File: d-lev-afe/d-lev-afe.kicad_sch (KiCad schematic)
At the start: 26 parts, among them J1 S8B-PH-SM4-TB, Q1 MMBT3904, Q2 MMBT3906, U1 74AHC04, U2 HT7533-1-SOT89, U3 SRV05-4

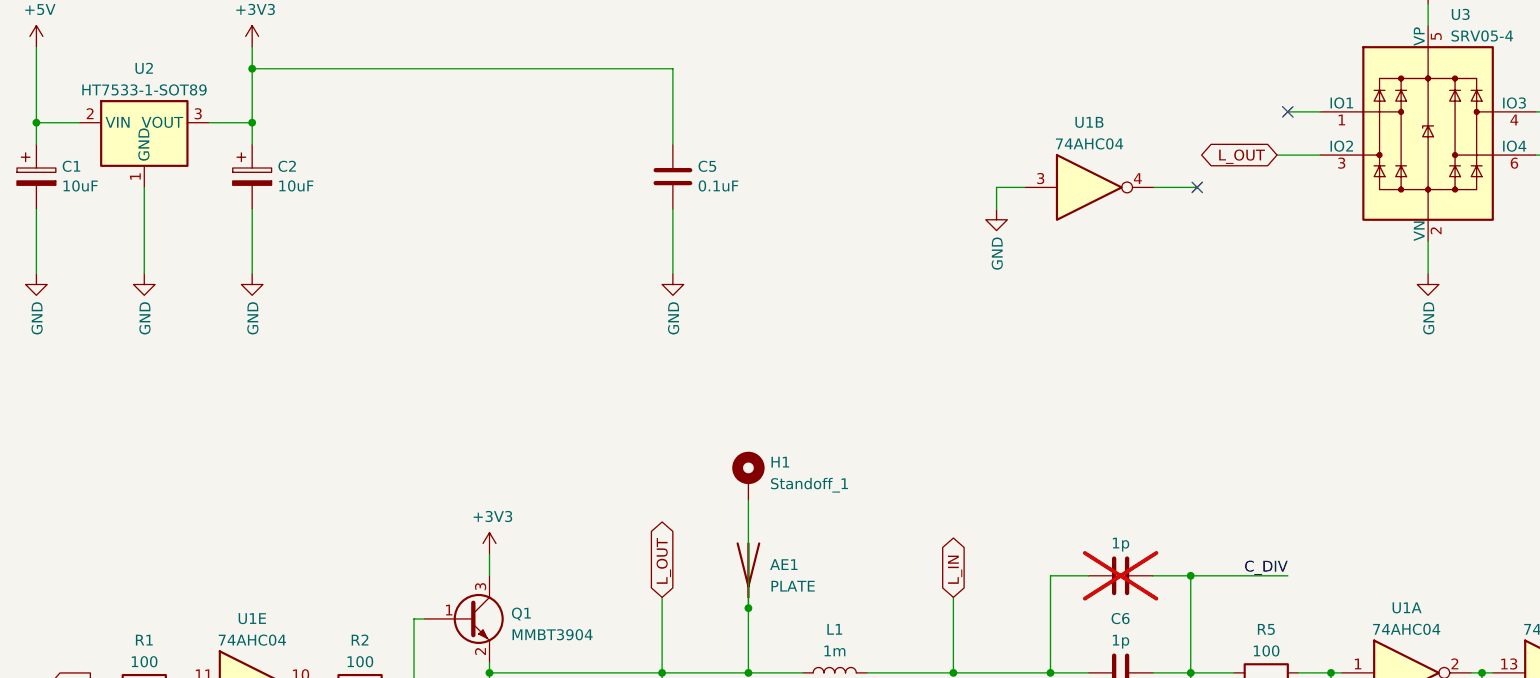
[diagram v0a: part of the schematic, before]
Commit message: clean up 3d models
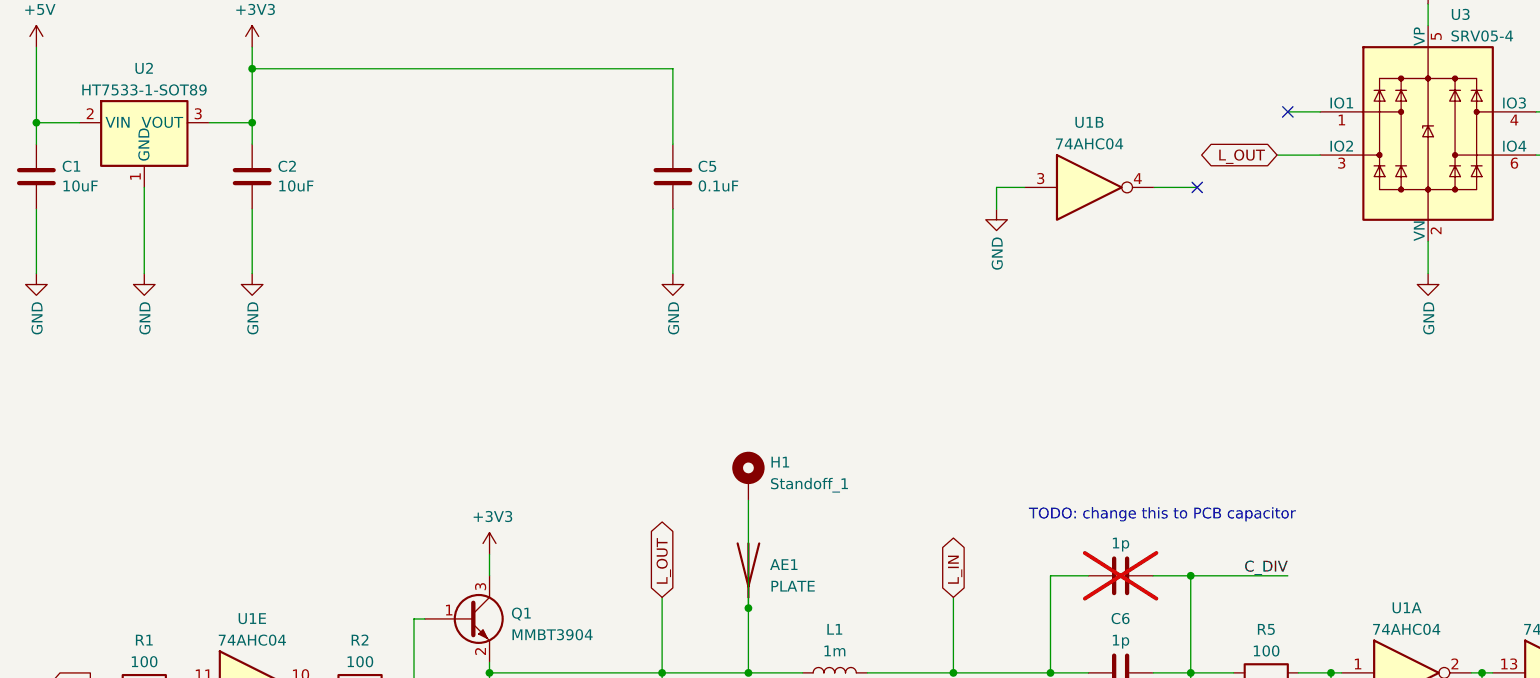
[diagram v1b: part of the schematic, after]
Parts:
- C1, C2: footprint Capacitor_Tantalum_SMD:CP_EIA-3216-18_Kemet-A -> Capacitor_SMD:C_0603_1608Metric; symbol Device:CP -> Device:C
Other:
- note added: "TODO: change this to PCB capacitor"

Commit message: many many changes'
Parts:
- removed C8: 1p, Capacitor_SMD:C_0805_2012Metric_Pad1.18x1.45mm_HandSolder, symbol Device:C
- added AE2: PLATE, theremin:keystone-PN5331TR, symbol Device:Antenna
- added H4, H5: Standoff_2, theremin:SMTSO-M4, symbol Mechanical:MountingHole_Pad
- AE1: footprint (none) -> theremin:keystone-PN5331TR; now in the parts list
- C6: footprint Capacitor_SMD:C_0603_1608Metric -> theremin:testpoint_cap_1pf
- J1: footprint Connector_JST:JST_PH_S8B-PH-SM4-TB_1x08-1MP_P2.00mm_Horizontal -> theremin:JST_PH_S8B-PH-SM4-TB_1x08-1MP_P2.00mm_Horizontal; symbol Connector_Generic:Conn_01x08 -> assorted:Conn_01x08_MountingPin
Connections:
- net C_DIV: now also U3.3 (IO2); no longer U3.4 (IO3)
- net L_OUT: now also U3.4 (IO3), AE2.1 (A); no longer U3.3 (IO2)
- no-connect marks 5 -> 8
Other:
- note added: "TODO: change this to PCB adjustable capacitor"
- note added: "to do: replace with Keystone 1020?"
- note removed: "TODO: change this to PCB capacitor"
- moved on the sheet: AE1, C6

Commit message: many more changes
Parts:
- removed U2: HT7533-1-SOT89, Package_TO_SOT_SMD:SOT-89-3, symbol Regulator_Linear:HT75xx-1-SOT89
- added U4: AP2112K-3.3, Package_TO_SOT_SMD:SOT-23-5, symbol Regulator_Linear:AP2112K-3.3
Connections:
- net +3V3: now also U4.5 (VOUT)
- net +5V: now also U4.1 (VIN), U4.3 (EN)
- net GND: now also U4.2 (GND)
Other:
- moved on the sheet: C1, C2
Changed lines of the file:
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@@
   (junction (at 142.24 111.76) (diameter 0) (color 0 0 0 0)
+  )
+  (junction (at 34.29 49.53) (diameter 0) (color 0 0 0 0)
   )
   (junction (at 118.11 104.14) (diameter 0) (color 0 0 0 0)
@@
     (stroke (width 0) (type default))
   )
+  (wire (pts (xy 46.99 57.15) (xy 46.99 66.675))
+    (stroke (width 0) (type default))
+  )
   (wire (pts (xy 40.64 113.03) (xy 43.18 113.03))
     (stroke (width 0) (type default))
@@
     (stroke (width 0) (type default))
   )
-  (wire (pts (xy 34.29 57.15) (xy 34.29 64.77))
+  (wire (pts (xy 34.29 61.595) (xy 34.29 64.77))
     (stroke (width 0) (type default))
   )
@@
     (stroke (width 0) (type default))
   )
-  (wire (pts (xy 59.69 49.53) (xy 59.69 46.99))
+  (wire (pts (xy 59.69 53.975) (xy 59.69 46.99))
     (stroke (width 0) (type default))
   )
@@
     (stroke (width 0) (type default))
   )
+  (wire (pts (xy 34.29 49.53) (xy 34.29 53.975))
+    (stroke (width 0) (type default))
+  )
   (wire (pts (xy 228.6 64.77) (xy 245.11 64.77))
     (stroke (width 0) (type default))
   )
+  (wire (pts (xy 39.37 49.53) (xy 34.29 49.53))
+    (stroke (width 0) (type default))
+  )
   (wire (pts (xy 87.63 97.79) (xy 87.63 100.33))
     (stroke (width 0) (type default))
   )
-  (wire (pts (xy 59.69 57.15) (xy 59.69 64.77))
+  (wire (pts (xy 59.69 61.595) (xy 59.69 64.77))
     (stroke (width 0) (type default))
   )
@@
   )
   (wire (pts (xy 77.47 162.56) (xy 77.47 165.1))
-    (stroke (width 0) (type default))
-  )
-  (wire (pts (xy 46.99 54.61) (xy 46.99 64.77))
     (stroke (width 0) (type default))
   )
@@
     )
   )
-  (symbol (lib_id "Device:C") (at 59.69 53.34 0) (unit 1)
-    (in_bom yes) (on_board yes) (dnp no)
-    (property "Reference" "C2" (at 62.6872 52.1716 0)
-      (effects (font (size 1.27 1.27)) (justify left))
-    )
-    (property "Value" "10uF" (at 62.6872 54.483 0)
-      (effects (font (size 1.27 1.27)) (justify left))
-    )
-    (property "Footprint" "Capacitor_SMD:C_0603_1608Metric" (at 60.6552 57.15 0)
-      (effects (font (size 1.27 1.27)) hide)
-    )
-    (property "Datasheet" "~" (at 59.69 53.34 0)
+  (symbol (lib_id "Device:C") (at 59.69 57.785 0) (unit 1)
+    (in_bom yes) (on_board yes) (dnp no)
+    (property "Reference" "C2" (at 62.6872 56.6166 0)
+      (effects (font (size 1.27 1.27)) (justify left))
+    )
+    (property "Value" "10uF" (at 62.6872 58.928 0)
+      (effects (font (size 1.27 1.27)) (justify left))
+    )
+    (property "Footprint" "Capacitor_SMD:C_0603_1608Metric" (at 60.6552 61.595 0)
+      (effects (font (size 1.27 1.27)) hide)
+    )
+    (property "Datasheet" "~" (at 59.69 57.785 0)
       (effects (font (size 1.27 1.27)) hide)
     )
@@
     )
   )
-  (symbol (lib_id "Regulator_Linear:HT75xx-1-SOT89") (at 46.99 49.53 0) (unit 1)
-    (in_bom yes) (on_board yes) (dnp no) (fields_autoplaced)
-    (property "Reference" "U2" (at 46.99 40.64 0)
-      (effects (font (size 1.27 1.27)))
-    )
-    (property "Value" "HT7533-1-SOT89" (at 46.99 43.18 0)
-      (effects (font (size 1.27 1.27)))
-    )
-    (property "Footprint" "Package_TO_SOT_SMD:SOT-89-3" (at 46.99 41.275 0)
-      (effects (font (size 1.27 1.27) italic) hide)
-    )
-    (property "Datasheet" "https://www.holtek.com/documents/10179/116711/HT75xx-1v250.pdf" (at 46.99 46.99 0)
-      (effects (font (size 1.27 1.27)) hide)
-    )
-    (pin "1")
-    (pin "2")
-    (pin "3")
-    (instances
-      (project "d-lev-afe"
-        (path "/3b0ead2a-6fae-4ae2-8192-98c9e26989ec"
-          (reference "U2") (unit 1)
-        )
-      )
-    )
-  )
-  (symbol (lib_id "power:GND") (at 46.99 64.77 0) (unit 1)
-    (in_bom yes) (on_board yes) (dnp no)
-    (property "Reference" "#PWR03" (at 46.99 71.12 0)
-      (effects (font (size 1.27 1.27)) hide)
-    )
-    (property "Value" "GND" (at 47.117 68.0212 90)
+  (symbol (lib_id "power:GND") (at 46.99 66.675 0) (unit 1)
+    (in_bom yes) (on_board yes) (dnp no)
+    (property "Reference" "#PWR03" (at 46.99 73.025 0)
+      (effects (font (size 1.27 1.27)) hide)
+    )
+    (property "Value" "GND" (at 47.117 69.9262 90)
       (effects (font (size 1.27 1.27)) (justify right))
     )
-    (property "Footprint" "" (at 46.99 64.77 0)
-      (effects (font (size 1.27 1.27)) hide)
-    )
-    (property "Datasheet" "" (at 46.99 64.77 0)
+    (property "Footprint" "" (at 46.99 66.675 0)
+      (effects (font (size 1.27 1.27)) hide)
+    )
+    (property "Datasheet" "" (at 46.99 66.675 0)
       (effects (font (size 1.27 1.27)) hide)
     )
@@
     )
   )
+  (symbol (lib_id "Regulator_Linear:AP2112K-3.3") (at 46.99 49.53 0) (unit 1)
+    (in_bom yes) (on_board yes) (dnp no) (fields_autoplaced)
+    (property "Reference" "U4" (at 46.99 40.64 0)
+      (effects (font (size 1.27 1.27)))
+    )
+    (property "Value" "AP2112K-3.3" (at 46.99 43.18 0)
+      (effects (font (size 1.27 1.27)))
+    )
+    (property "Footprint" "Package_TO_SOT_SMD:SOT-23-5" (at 46.99 41.275 0)
+      (effects (font (size 1.27 1.27)) hide)
+    )
+    (property "Datasheet" "https://www.diodes.com/assets/Datasheets/AP2112.pdf" (at 46.99 46.99 0)
+      (effects (font (size 1.27 1.27)) hide)
+    )
+    (pin "1")
+    (pin "2")
+    (pin "3")
+    (pin "4")
+    (pin "5")
+    (instances
+      (project "d-lev-afe"
+        (path "/3b0ead2a-6fae-4ae2-8192-98c9e26989ec"
+          (reference "U4") (unit 1)
+        )
+      )
+    )
+  )
   (symbol (lib_id "power:GND") (at 228.6 88.9 0) (unit 1)
     (in_bom yes) (on_board yes) (dnp no)
@@
     )
   )
-  (symbol (lib_id "Device:C") (at 34.29 53.34 0) (unit 1)
-    (in_bom yes) (on_board yes) (dnp no)
-    (property "Reference" "C1" (at 37.2872 52.1716 0)
-      (effects (font (size 1.27 1.27)) (justify left))
-    )
-    (property "Value" "10uF" (at 37.2872 54.483 0)
-      (effects (font (size 1.27 1.27)) (justify left))
-    )
-    (property "Footprint" "Capacitor_SMD:C_0603_1608Metric" (at 35.2552 57.15 0)
-      (effects (font (size 1.27 1.27)) hide)
-    )
-    (property "Datasheet" "~" (at 34.29 53.34 0)
-      (effects (font (size 1.27 1.27)) hide)
-    )
+  (symbol (lib_id "Device:C") (at 34.29 57.785 0) (unit 1)
+    (in_bom yes) (on_board yes) (dnp no)
+    (property "Reference" "C1" (at 37.2872 56.6166 0)
+      (effects (font (size 1.27 1.27)) (justify left))
+    )
+    (property "Value" "10uF" (at 37.2872 58.928 0)
+      (effects (font (size 1.27 1.27)) (justify left))
+    )
+    (property "Footprint" "Capacitor_SMD:C_0603_1608Metric" (at 35.2552 61.595 0)
+      (effects (font (size 1.27 1.27)) hide)
+    )
+    (property "Datasheet" "~" (at 34.29 57.785 0)
+      (effects (font (size 1.27 1.27)) hide)
+    )
